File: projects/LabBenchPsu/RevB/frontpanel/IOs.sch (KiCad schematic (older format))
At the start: 26 parts, among them P17 NHD-1.69-160128UGC3, U8 MCP23017

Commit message: working on schematic and footprints
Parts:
- P17: footprint (none) -> frep:NHD-1.69-160128UGC3
- R10, R11, R12, R13, R14, R15, R16, R17, R19, R20, R21, R22, R8, R9: footprint (none) -> frep:R0805
- S1, S2, S3, S4: footprint (none) -> frep:TACTILE-PTH
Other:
- note added: "Input"
- note added: "Output"
- moved on the sheet: C10, C11, C8, C9, ENC1, ENC2, P17, R10, R11, R12, R13, R14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

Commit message: start with pcb
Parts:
- U8: footprint (none) -> frep:SOIC28W
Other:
- note added: "GPIO expander"
- note added: "OLED display"
- note added: "rotary encoder"
- note removed: "display"
- moved on the sheet: C10, C11, C8, C9, ENC1, ENC2, P17, R14, R15, R16, R17, R19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

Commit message: pcb in progress
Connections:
- net B1: now also U8.21 (GPA0); no longer U8.23 (GPA2)
- net B2: now also U8.24 (GPA3); no longer U8.26 (GPA5)
- net SW1: now also U8.23 (GPA2); no longer U8.21 (GPA0)
- net SW2: now also U8.26 (GPA5); no longer U8.24 (GPA3)
- net loadOn: now reaches U8.5 (GPB4)
- no-connect marks 12 -> 11
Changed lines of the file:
@@
 Text Notes 2950 3725 0    60   ~ 0
 i2c slave address: 0x20
-Text GLabel 4200 2750 2    40   Input ~ 0
+Text GLabel 4200 2550 2    40   Input ~ 0
 SW1
 Text GLabel 4200 2650 2    40   Input ~ 0
 A1
-Text GLabel 4200 2550 2    40   Input ~ 0
+Text GLabel 4200 2750 2    40   Input ~ 0
 B1
-Text GLabel 4200 2450 2    40   Input ~ 0
+Text GLabel 4200 2250 2    40   Input ~ 0
 SW2
 Text GLabel 4200 2350 2    40   Input ~ 0
 A2
-Text GLabel 4200 2250 2    40   Input ~ 0
+Text GLabel 4200 2450 2    40   Input ~ 0
 B2
 NoConn ~ 4200 2150
@@
 Text GLabel 2700 2150 0    40   Input ~ 0
 But2
-NoConn ~ 2700 2450
 NoConn ~ 2700 2550
 NoConn ~ 2700 2650
@@
 Wire Notes Line
 	8055 5150 8055 475
+Text GLabel 2700 2450 0    40   Input ~ 0
+loadOn
 $EndSCHEMATC

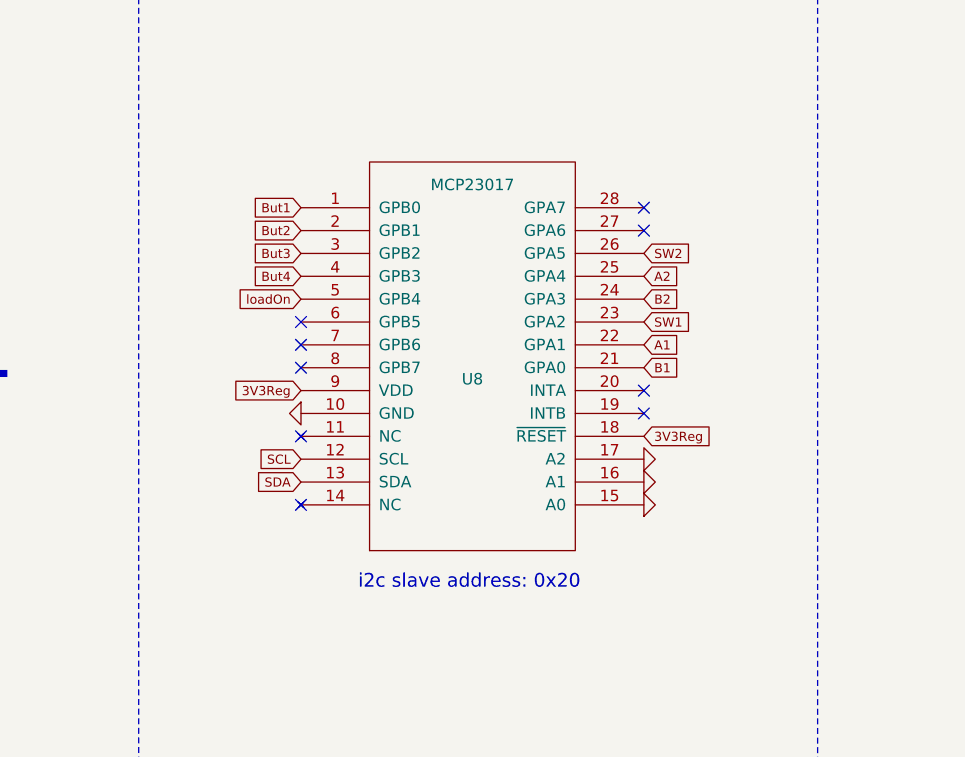
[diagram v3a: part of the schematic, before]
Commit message: protective diodes added
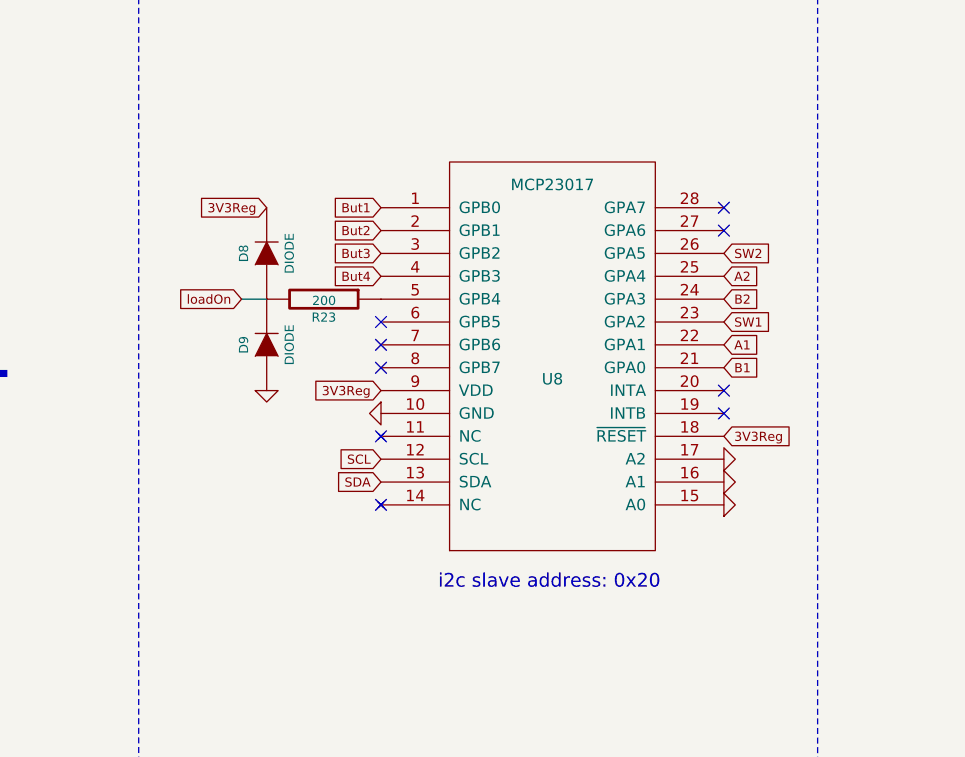
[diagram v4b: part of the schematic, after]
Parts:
- added D8, D9: DIODE, frep:Diode-MiniMELF_Handsoldering, symbol DIODE
- added R23: 200, frep:R0805, symbol R
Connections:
- net 3V3Reg: now also D8.2 (K)
- net GND: now also D9.1 (A)
- net loadOn: now also D8.1 (A), D9.2 (K), R23.2; no longer U8.5 (GPB4)
- new net: R23.1, U8.5 (GPB4)
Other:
- moved on the sheet: U8
